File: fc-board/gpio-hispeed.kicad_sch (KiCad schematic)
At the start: 6 parts, among them J7 685119134923, U8 RT9742SNGV

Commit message: Removed zips; updated gitignore
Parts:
- renumbered U8 to U9
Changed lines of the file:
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@@
 		(dnp no)
 		(fields_autoplaced yes)
-		(property "Reference" "U8"
+		(property "Reference" "U9"
 			(at 240.03 101.6 0)
 			(effects
@@
 			(project ""
 				(path "/14bbabed-904f-4efc-8ba4-be00e59385c4/edd7e4f6-7524-424d-ae74-0eda33819a09"
-					(reference "U8")
+					(reference "U9")
 					(unit 1)
 				)

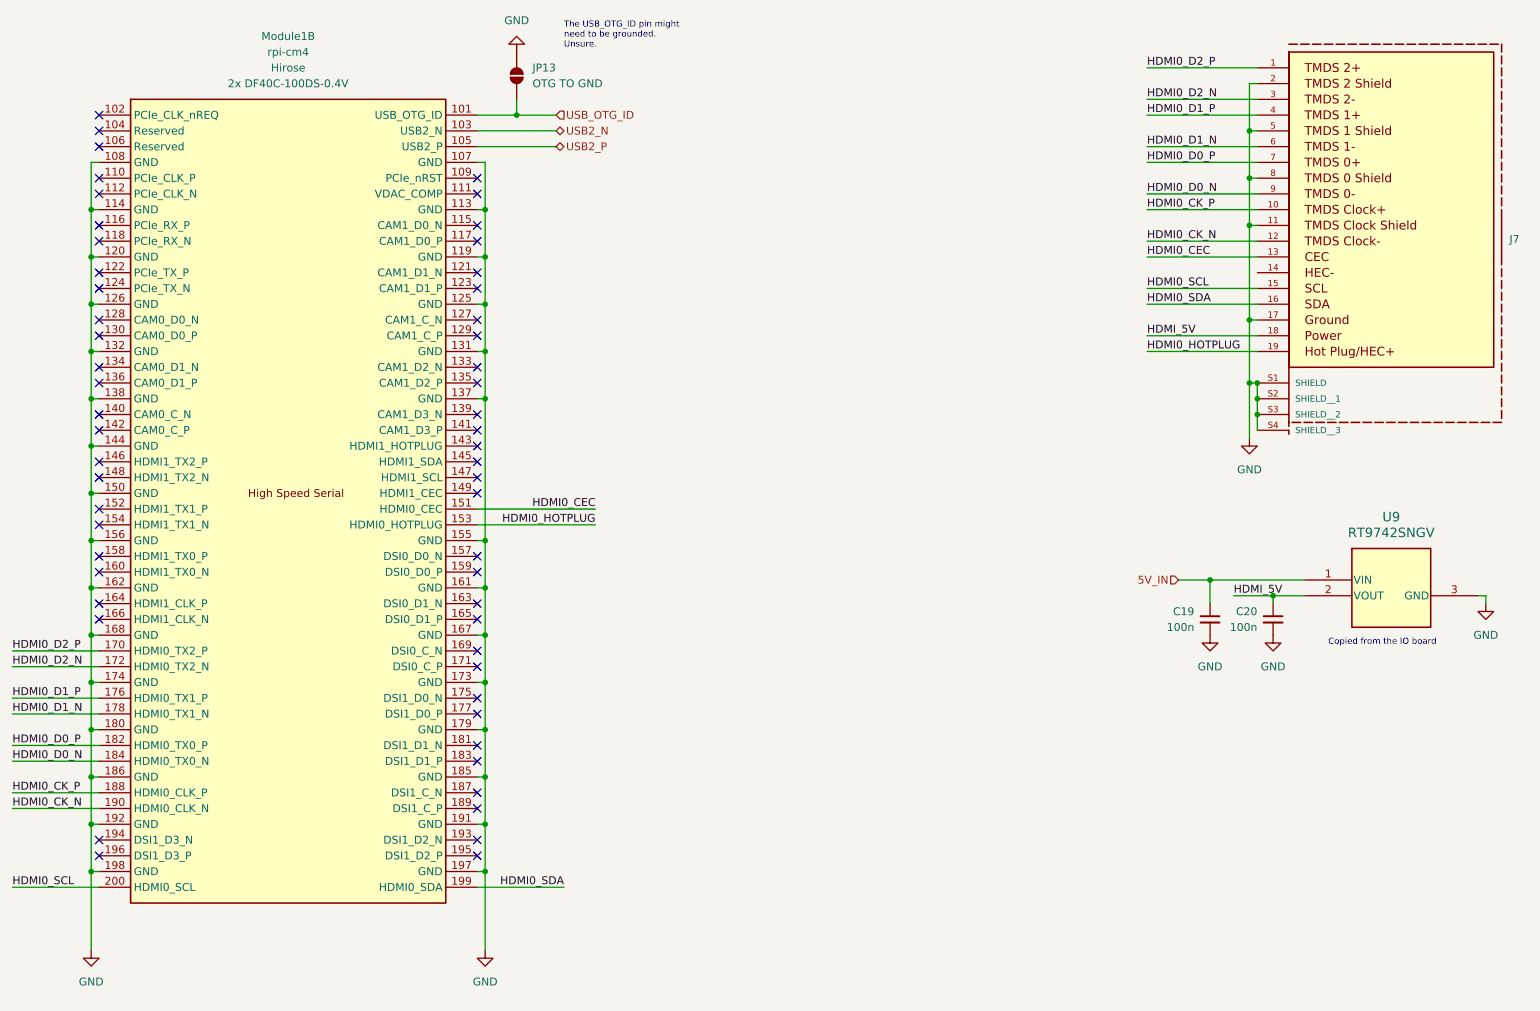
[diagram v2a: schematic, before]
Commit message: Fc board (#9)
* FC board updates

* Finished routing; cleaned library

* Updated RJ45 jack

* Assigned part numbers to everything, replaced ethernet jack

* Finalized layout

* V1 sent for printing
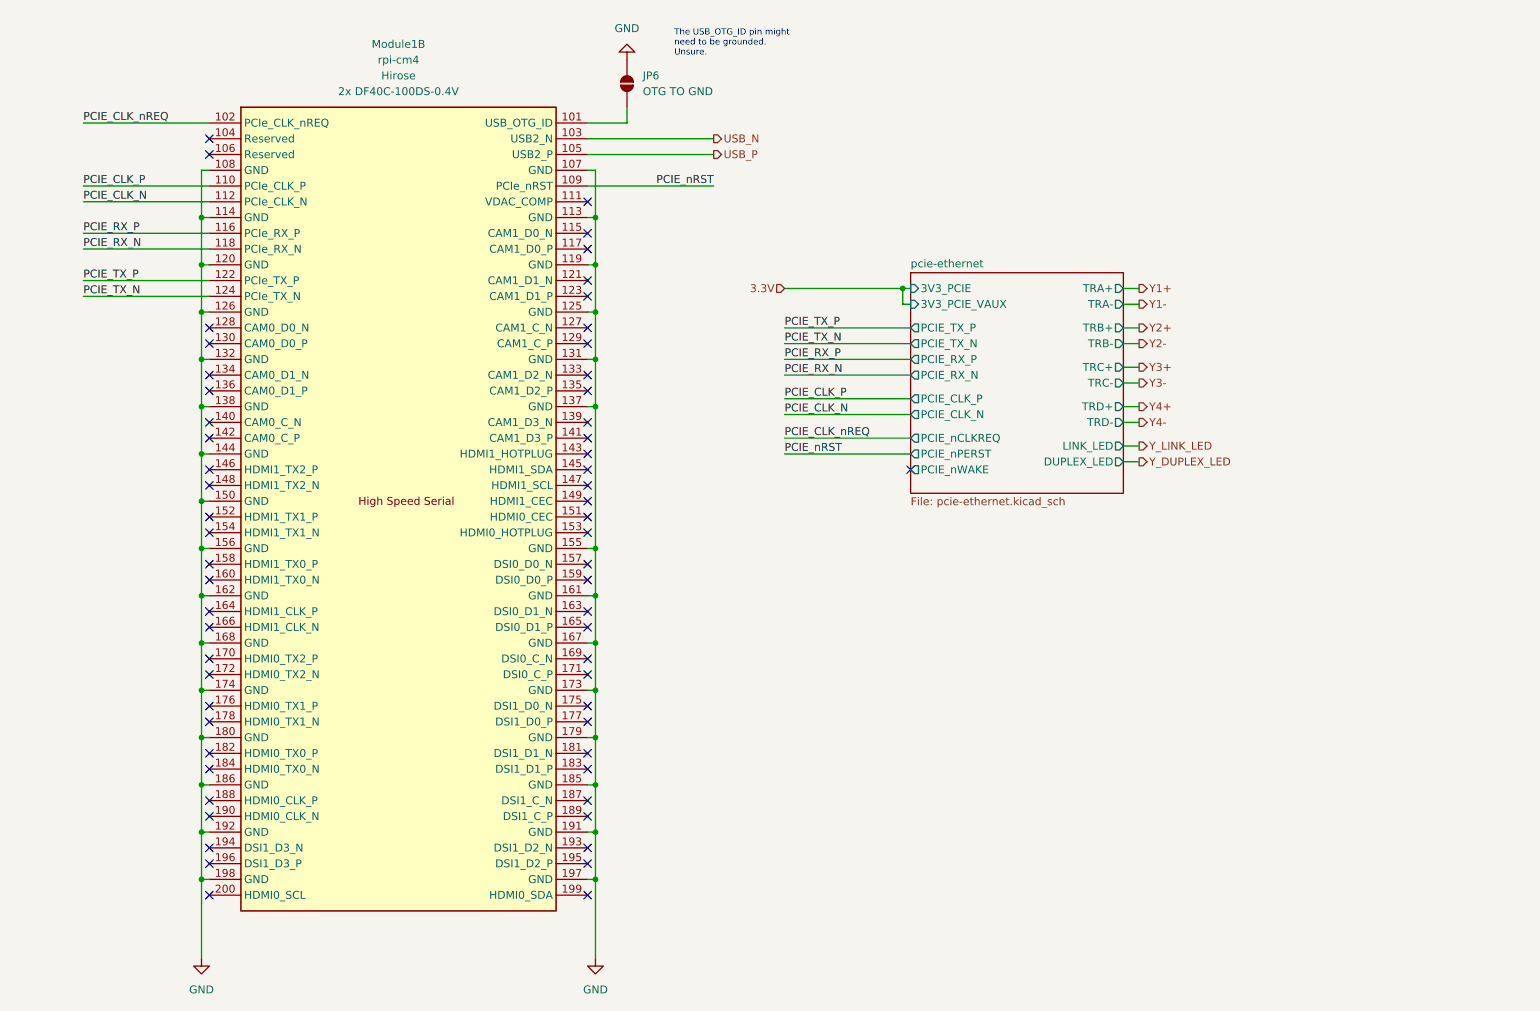
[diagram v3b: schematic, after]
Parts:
- removed C19, C20: 100n, Capacitor_SMD:C_1206_3216Metric, symbol Device:C_Small
- removed J7: 685119134923, fc-board:685119134923, symbol fc-board:685119134923
- removed JP13: OTG TO GND, Jumper:SolderJumper-2_P1.3mm_Open_Pad1.0x1.5mm, symbol Jumper:SolderJumper_2_Open
- removed U9: RT9742SNGV, fc-board:RT9742SNGV, symbol fc-board:RT9742SNGV
- added JP6: OTG TO GND, Jumper:SolderJumper-2_P1.3mm_Open_Pad1.0x1.5mm, symbol Jumper:SolderJumper_2_Open
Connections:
- net GND: now also JP6.2 (B)
- net PCIE_CLK_nREQ: now reaches Module1.102 (PCIe_CLK_nREQ)
- net PCIE_nRST: now reaches Module1.109 (PCIe_nRST)
- net PCIE_CLK_P: now reaches Module1.110 (PCIe_CLK_P)
- net PCIE_CLK_N: now reaches Module1.112 (PCIe_CLK_N)
- net PCIE_RX_P: now reaches Module1.116 (PCIe_RX_P)
- net PCIE_RX_N: now reaches Module1.118 (PCIe_RX_N)
- net PCIE_TX_P: now reaches Module1.122 (PCIe_TX_P)
- net PCIE_TX_N: now reaches Module1.124 (PCIe_TX_N)
- net HDMI0_CEC: no longer names the net of Module1.151 (HDMI0_CEC)
- net HDMI0_CK_N: no longer names the net of Module1.190 (HDMI0_CLK_N)
- net HDMI0_CK_P: no longer names the net of Module1.188 (HDMI0_CLK_P)
- net HDMI0_D0_N: no longer names the net of Module1.184 (HDMI0_TX0_N)
- net HDMI0_D0_P: no longer names the net of Module1.182 (HDMI0_TX0_P)
- net HDMI0_D1_N: no longer names the net of Module1.178 (HDMI0_TX1_N)
- net HDMI0_D1_P: no longer names the net of Module1.176 (HDMI0_TX1_P)
- net HDMI0_D2_N: no longer names the net of Module1.172 (HDMI0_TX2_N)
- net HDMI0_D2_P: no longer names the net of Module1.170 (HDMI0_TX2_P)
- net HDMI0_HOTPLUG: no longer names the net of Module1.153 (HDMI0_HOTPLUG)
- net HDMI0_SCL: no longer names the net of Module1.200 (HDMI0_SCL)
- net HDMI0_SDA: no longer names the net of Module1.199 (HDMI0_SDA)
- net USB2_N renamed USB_N
- net USB2_P renamed USB_P
- net USB_OTG_ID: no longer names the net of Module1.101 (USB_OTG_ID)
- net USB_OTG_ID: now also JP6.1 (A)
- no-connect marks 55 -> 60
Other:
- added sheet pcie-ethernet (pcie-ethernet.kicad_sch)
- note removed: "Copied from the IO board"
- moved on the sheet: Module1B

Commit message: Fixed incorrect routes, modified gondola eth, cosmetics
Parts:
- renumbered JP6 to JP9
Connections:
- net PCIE_CLK_N renamed PI_PCIE_CLK_N
- net PCIE_CLK_P renamed PI_PCIE_CLK_P
- net PCIE_RX_N renamed PI_PCIE_RX_N
- net PCIE_RX_P renamed PI_PCIE_RX_P
- net PCIE_TX_N renamed PI_PCIE_TX_N
- net PCIE_TX_P renamed PI_PCIE_TX_P
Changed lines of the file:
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@@
 	(title_block
 		(title "CM4 Hi-speed Serial")
-		(date "2025-10-20")
+		(date "2025-12-08")
 		(rev "0.1")
 	)
@@
 		)
 	)
-	(label "PCIE_CLK_N"
+	(label "PI_PCIE_CLK_N"
 		(at 142.24 85.09 0)
 		(effects
@@
 		)
 	)
-	(label "PCIE_TX_P"
+	(label "PI_PCIE_TX_P"
 		(at 29.21 63.5 0)
 		(effects
@@
 		)
 	)
-	(label "PCIE_RX_N"
+	(label "PI_PCIE_RX_N"
 		(at 29.21 58.42 0)
 		(effects
@@
 		)
 	)
-	(label "PCIE_CLK_P"
+	(label "PI_PCIE_CLK_P"
 		(at 142.24 82.55 0)
 		(effects
@@
 		)
 	)
-	(label "PCIE_RX_N"
-		(at 142.24 78.74 0)
+	(label "PI_PCIE_RX_N"
+		(at 142.24 73.66 0)
 		(effects
 			(font
@@
 		)
 	)
-	(label "PCIE_RX_P"
-		(at 142.24 76.2 0)
+	(label "PI_PCIE_RX_P"
+		(at 142.24 71.12 0)
 		(effects
 			(font
@@
 		)
 	)
-	(label "PCIE_CLK_P"
+	(label "PI_PCIE_CLK_P"
 		(at 29.21 48.26 0)
 		(effects
@@
 		)
 	)
-	(label "PCIE_TX_N"
-		(at 142.24 73.66 0)
+	(label "PI_PCIE_TX_N"
+		(at 142.24 78.74 0)
 		(effects
 			(font
@@
 		)
 	)
-	(label "PCIE_TX_N"
+	(label "PI_PCIE_TX_N"
 		(at 29.21 66.04 0)
 		(effects
@@
 		)
 	)
-	(label "PCIE_RX_P"
+	(label "PI_PCIE_RX_P"
 		(at 29.21 55.88 0)
 		(effects
@@
 		)
 	)
-	(label "PCIE_CLK_N"
+	(label "PI_PCIE_CLK_N"
 		(at 29.21 50.8 0)
 		(effects
@@
 		)
 	)
-	(label "PCIE_TX_P"
-		(at 142.24 71.12 0)
+	(label "PI_PCIE_TX_P"
+		(at 142.24 76.2 0)
 		(effects
 			(font
@@
 		(dnp no)
 		(fields_autoplaced yes)
-		(property "Reference" "#PWR027"
+		(property "Reference" "#PWR024"
 			(at 116.84 21.59 0)
 			(effects
@@
 			(project ""
 				(path "/14bbabed-904f-4efc-8ba4-be00e59385c4/edd7e4f6-7524-424d-ae74-0eda33819a09"
-					(reference "#PWR027")
+					(reference "#PWR024")
 					(unit 1)
 				)
@@
 		(dnp no)
 		(fields_autoplaced yes)
-		(property "Reference" "#PWR025"
+		(property "Reference" "#PWR022"
 			(at 48.26 179.07 0)
 			(effects
@@
 			(project "fc-board"
 				(path "/14bbabed-904f-4efc-8ba4-be00e59385c4/edd7e4f6-7524-424d-ae74-0eda33819a09"
-					(reference "#PWR025")
+					(reference "#PWR022")
 					(unit 1)
 				)
@@
 		(dnp no)
 		(fields_autoplaced yes)
-		(property "Reference" "#PWR026"
+		(property "Reference" "#PWR023"
 			(at 111.76 179.07 0)
 			(effects
@@
 			(project "fc-board"
 				(path "/14bbabed-904f-4efc-8ba4-be00e59385c4/edd7e4f6-7524-424d-ae74-0eda33819a09"
-					(reference "#PWR026")
+					(reference "#PWR023")
 					(unit 1)
 				)
@@
 		(dnp no)
 		(fields_autoplaced yes)
-		(property "Reference" "JP6"
+		(property "Reference" "JP9"
 			(at 119.38 30.4799 90)
 			(effects
@@
 			(project ""
 				(path "/14bbabed-904f-4efc-8ba4-be00e59385c4/edd7e4f6-7524-424d-ae74-0eda33819a09"
-					(reference "JP6")
+					(reference "JP9")
 					(unit 1)
 				)

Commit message: Fleshed out part numbers and design rules
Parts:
- Module1: Field5 2x DF40C-100DS-0.4V -> (none)
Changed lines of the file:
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@@
 			)
 		)
-		(property "Datasheet" ""
+		(property "Datasheet" "https://www.hirose.com/en/product/document?clcode=&productname=&series=DF40&documenttype=Catalog&lang=en&documentid=en_DF40_CAT"
 			(at 82.55 125.73 0)
 			(effects
@@
 			)
 		)
-		(property "Description" ""
+		(property "Description" "DF40C-100DS-0.4V(51)"
 			(at -59.69 99.06 0)
 			(effects
@@
 			)
 		)
-		(property "Field5" "2x DF40C-100DS-0.4V"
-			(at 80.01 33.02 0)
-			(effects
-				(font
-					(size 1.27 1.27)
-				)
-			)
-		)
-		(property "Check_prices" ""
-			(at -59.69 99.06 0)
-			(effects
-				(font
-					(size 1.27 1.27)
-				)
-				(hide yes)
-			)
-		)
-		(property "DATASHEET-URL" ""
-			(at -59.69 99.06 0)
-			(effects
-				(font
-					(size 1.27 1.27)
-				)
-				(hide yes)
-			)
-		)
-		(property "GERDER" ""
-			(at -59.69 99.06 0)
-			(effects
-				(font
-					(size 1.27 1.27)
-				)
-				(hide yes)
-			)
-		)
-		(property "MOUNT" ""
-			(at -59.69 99.06 0)
-			(effects
-				(font
-					(size 1.27 1.27)
-				)
-				(hide yes)
-			)
-		)
-		(property "PART-NUMBER" ""
-			(at -59.69 99.06 0)
-			(effects
-				(font
-					(size 1.27 1.27)
-				)
-				(hide yes)
-			)
-		)
-		(property "PINS" ""
-			(at -59.69 99.06 0)
-			(effects
-				(font
-					(size 1.27 1.27)
-				)
-				(hide yes)
-			)
-		)
-		(property "RATED-CURRENT" ""
-			(at -59.69 99.06 0)
-			(effects
-				(font
-					(size 1.27 1.27)
-				)
-				(hide yes)
-			)
-		)
-		(property "SnapEDA_Link" ""
-			(at -59.69 99.06 0)
-			(effects
-				(font
-					(size 1.27 1.27)
-				)
-				(hide yes)
-			)
-		)
-		(property "TYPE" ""
-			(at -59.69 99.06 0)
-			(effects
-				(font
-					(size 1.27 1.27)
-				)
-				(hide yes)
-			)
-		)
-		(property "WORKING-VOLTAGE" ""
-			(at -59.69 99.06 0)
-			(effects
-				(font
-					(size 1.27 1.27)
-				)
-				(hide yes)
-			)
-		)
-		(property "CREATOR" ""
-			(at -59.69 99.06 0)
-			(effects
-				(font
-					(size 1.27 1.27)
-				)
-				(hide yes)
-			)
-		)
-		(property "Field6" ""
-			(at -59.69 99.06 0)
-			(effects
-				(font
-					(size 1.27 1.27)
-				)
-				(hide yes)
-			)
-		)
-		(property "Field7" ""
-			(at -59.69 99.06 0)
-			(effects
-				(font
-					(size 1.27 1.27)
-				)
-				(hide yes)
-			)
-		)
-		(property "Field8" ""
-			(at -59.69 99.06 0)
-			(effects
-				(font
-					(size 1.27 1.27)
-				)
-				(hide yes)
-			)
-		)
-		(property "Part Description" ""
-			(at -59.69 99.06 0)
-			(effects
-				(font
-					(size 1.27 1.27)
-				)
-				(hide yes)
-			)
-		)
-		(property "VERIFIER" ""
-			(at -59.69 99.06 0)
-			(effects
-				(font
-					(size 1.27 1.27)
-				)
-				(hide yes)
-			)
-		)
